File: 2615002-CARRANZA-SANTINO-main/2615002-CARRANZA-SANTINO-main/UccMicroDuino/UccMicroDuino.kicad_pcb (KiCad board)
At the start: 2 copper layers, 14 parts, among them J1 USB_A, J2 Header, U1 ATtiny85-20SU

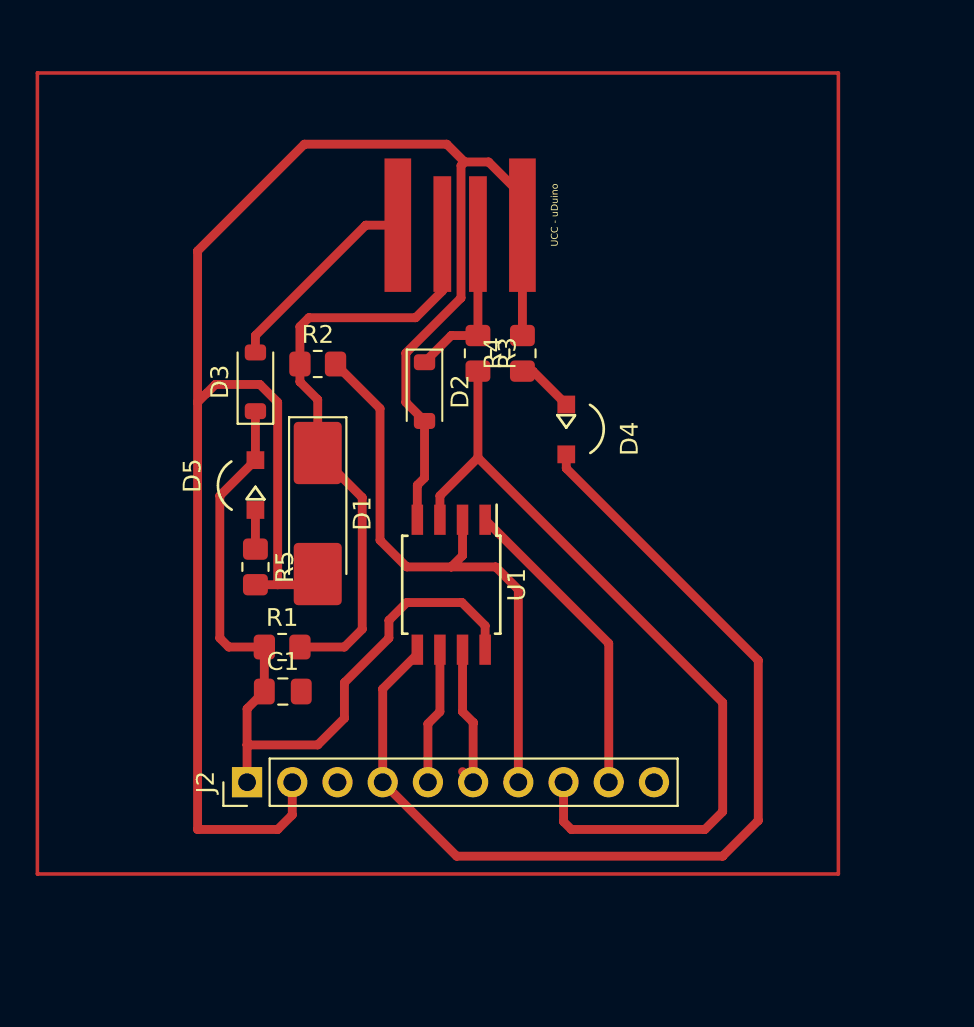
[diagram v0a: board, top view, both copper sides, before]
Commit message: 2615002- correcion de la placa kicad
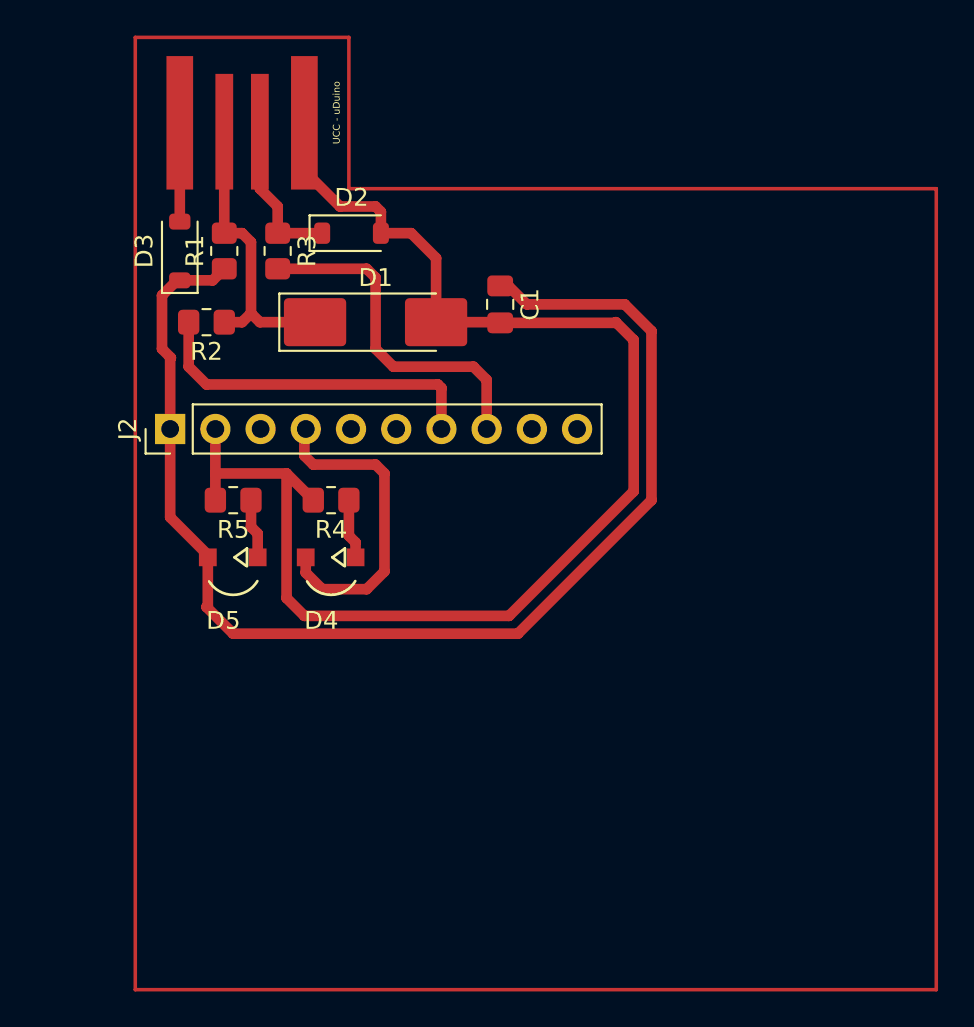
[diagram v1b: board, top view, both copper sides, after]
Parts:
- removed U1: ATtiny85-20SU, Package_SO:SOIC-8W_5.3x5.3mm_P1.27mm
- moved C1 24.9 mm to (101.0, 95.5), turned to -90 degrees
- moved R1 22.5 mm to (85.5, 92.5), turned to 90 degrees
- moved J2 20.3 mm to (82.5, 102.5)
- moved D4 15.2 mm to (91.1, 109.7), turned to 180 degrees
- moved R4 13.6 mm to (91.5, 106.5), turned to 180 degrees
- moved J1 13.5 mm to (86.5, 85.5)
- moved R3 12.6 mm to (88.5, 92.5)
- moved D1 11.2 mm to (94.0, 96.5), turned to 0 degrees
- moved D2 9.80 mm to (92.7, 91.5), turned to 0 degrees
- moved D3 8.49 mm to (83.0, 92.5)
- moved R2 6.68 mm to (84.5, 96.5), turned to 180 degrees
- moved D5 4.77 mm to (85.6, 109.7), turned to 180 degrees
- moved R5 3.95 mm to (86.0, 106.5), turned to 180 degrees
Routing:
- net Net-(D4-A): track 56.9 -> 18.0 mm
- net GND: track 111.2 -> 76.4 mm
- net Net-(J2-Pin_8): track 46.6 -> 19.4 mm
- net +5V: track 44.6 -> 70.5 mm
- net Net-(J2-Pin_9): track 17.6 -> 0.00 mm
- net Net-(D1-K): track 34.4 -> 16.9 mm
- net Net-(J2-Pin_7): track 33.6 -> 19.5 mm
- net Net-(J2-Pin_6): track 8.55 -> 0.34 mm
- net Net-(J2-Pin_5): track 7.72 -> 0.00 mm
- net Net-(D3-A): track 11.5 -> 5.55 mm
- net Net-(D5-K): track 2.20 -> 3.37 mm
- net Net-(D2-K): track 9.32 -> 8.61 mm

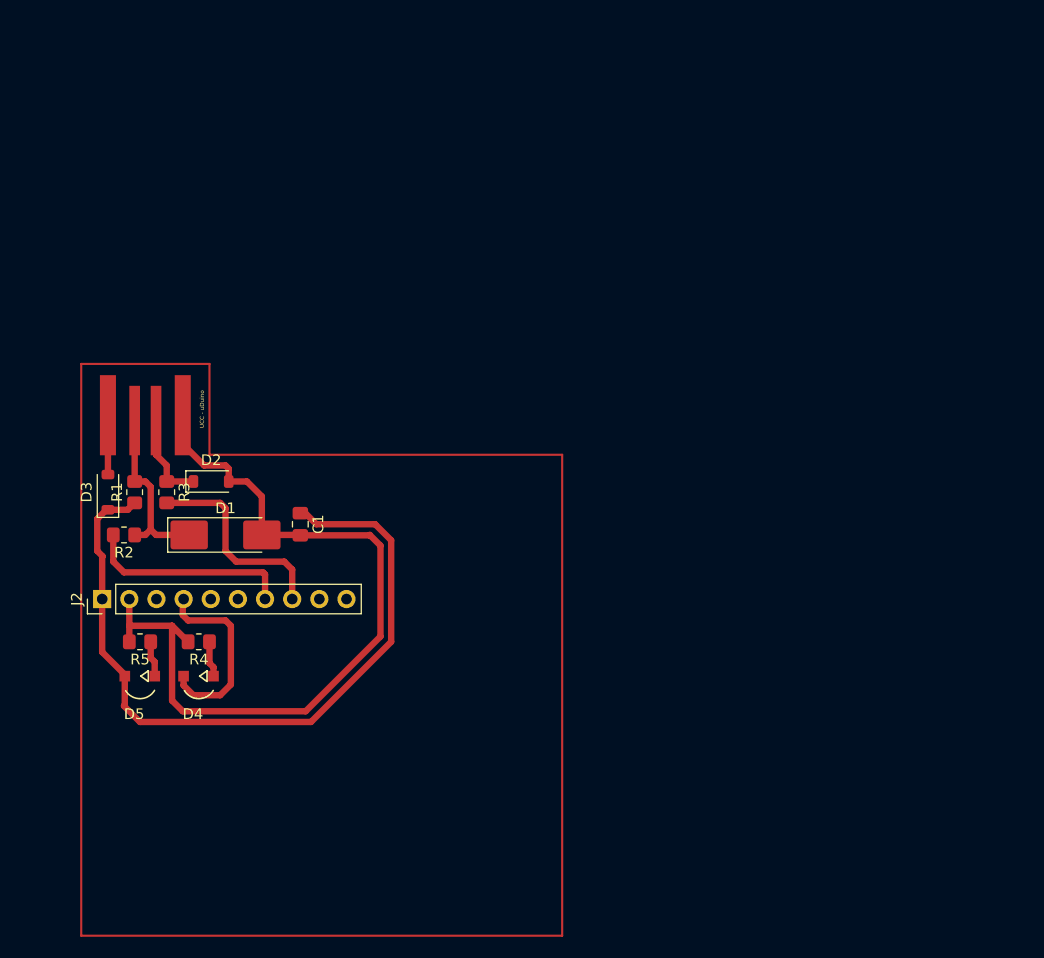
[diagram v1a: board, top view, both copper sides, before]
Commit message: 2615002-mi primer versionado de gitbash (correccion placa)
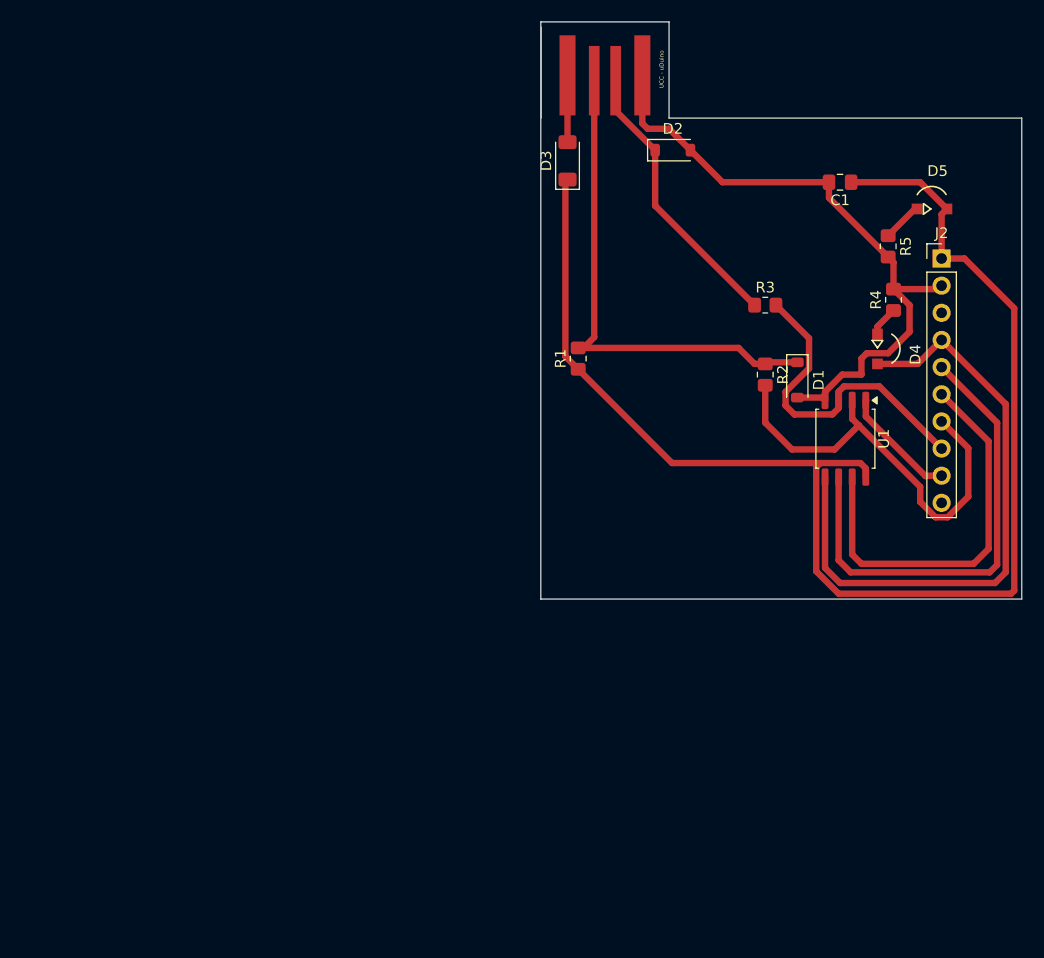
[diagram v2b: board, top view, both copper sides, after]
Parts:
- added U1: ATtiny85-20SU, Package_SO:SOIC-8_5.3x5.3mm_P1.27mm, F.Cu at (152.0, 87.5)
- D1: footprint Diode_SMD:D_MELF_Handsoldering -> Diode_SMD:D_SOD-123
- D3: footprint Diode_SMD:D_SOD-123 -> Diode_SMD:D_MiniMELF
- R5: value 33QQ 5% 1/8W -> 330Ω 5% 1/8W
- moved D5 86.7 mm to (160.5, 66.0), turned to 0 degrees
- moved J2 84.8 mm to (161.0, 70.6), turned to 0 degrees
- moved R5 79.2 mm to (156.0, 69.5), turned to -90 degrees
- moved R4 72.4 mm to (156.5, 74.5), turned to 90 degrees
- moved D4 70.7 mm to (155.0, 79.5), turned to -90 degrees
- moved R2 61.8 mm to (144.5, 81.5), turned to -90 degrees
- moved C1 59.8 mm to (151.5, 63.5), turned to 180 degrees
- moved R3 58.7 mm to (144.5, 75.0), turned to 0 degrees
- moved D1 55.4 mm to (147.5, 82.0), turned to -90 degrees
- moved J1 53.5 mm to (129.5, 53.7)
- moved D2 53.2 mm to (135.8, 60.5)
- moved D3 53.0 mm to (126.0, 61.5)
- moved R1 43.3 mm to (127.0, 80.0)
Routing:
- net +5V: track 70.5 -> 129.7 mm
- net Net-(J2-Pin_5): track 0.00 -> 44.0 mm
- net Net-(D4-A): track 18.0 -> 57.6 mm
- net Net-(J2-Pin_6): track 0.34 -> 37.2 mm
- net Net-(D1-K): track 16.9 -> 46.6 mm
- net Net-(J2-Pin_7): track 19.5 -> 40.3 mm
- net Net-(D2-K): track 8.61 -> 26.4 mm
- net GND: track 76.4 -> 60.6 mm
- net Net-(J2-Pin_8): track 19.4 -> 30.9 mm
- net Net-(J2-Pin_9): track 0.00 -> 11.0 mm
- net Net-(D3-A): track 5.55 -> 6.25 mm
- net Net-(D4-K): track 3.37 -> 2.82 mm
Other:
- board outline added: 45 x 54 mm

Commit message: 2615002- mi primer versionado con gitBash (placa finalizada)
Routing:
- net GND: track 60.6 -> 58.2 mm
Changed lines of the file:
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@@
-	)
-	(segment
-		(start 153.5 80)
-		(end 153.5 81.5)
-		(width 0.6)
-		(layer "F.Cu")
-		(net "GND")
-	)
-	(segment
-		(start 153.5 81.5)
-		(end 151.695001 81.5)
-		(width 0.6)
-		(layer "F.Cu")
-		(net "GND")
-	)
-	(segment
-		(start 156 79.5)
-		(end 154 79.5)
-		(width 0.6)
-		(layer "F.Cu")
-		(net "GND")
 	)
 	(segment
@@
 	)
 	(segment
-		(start 156.5 73.5)
-		(end 158 75)
+		(start 150.095 83.100001)
+		(end 151.695001 81.5)
 		(width 0.6)
 		(layer "F.Cu")
@@
 		(start 150.4625 64.9625)
 		(end 150.4625 63.5)
-		(width 0.6)
-		(layer "F.Cu")
-		(net "GND")
-	)
-	(segment
-		(start 158 75)
-		(end 158 77.5)
-		(width 0.6)
-		(layer "F.Cu")
-		(net "GND")
-	)
-	(segment
-		(start 154 79.5)
-		(end 153.5 80)
 		(width 0.6)
 		(layer "F.Cu")
@@
 	(segment
 		(start 151.695001 81.5)
-		(end 150.095 83.100001)
+		(end 153.5 81.5)
 		(width 0.6)
 		(layer "F.Cu")
@@
 	)
 	(segment
-		(start 150.095 83.100001)
-		(end 150.095 83.9125)
+		(start 153.5 81.5)
+		(end 153.5 76.5)
+		(width 0.6)
+		(layer "F.Cu")
+		(net "GND")
+	)
+	(segment
+		(start 153.5 76.5)
+		(end 156.5 73.5)
 		(width 0.6)
 		(layer "F.Cu")
@@
 		(start 160.68 73.5)
 		(end 161 73.18)
-		(width 0.6)
-		(layer "F.Cu")
-		(net "GND")
-	)
-	(segment
-		(start 158 77.5)
-		(end 156 79.5)
 		(width 0.6)
 		(layer "F.Cu")
@@
 		(width 0.6)
 		(layer "F.Cu")
+		(net "GND")
+	)
+	(segment
+		(start 150.095 83.9125)
+		(end 150.095 83.100001)
+		(width 0.6)
+		(layer "F.Cu")
